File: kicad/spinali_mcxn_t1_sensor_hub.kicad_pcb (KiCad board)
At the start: 2 copper layers, 25 parts, among them U11 BMP390, U13 SK9822-EC20, U14 MPM3822CGRH-Z, U15 TJA1462ATK, U16 PCMF3USB3S, U17 LM74700, U2 MIC5504-1.8YMT, U3 MIC28514T-E/PHA, U4 ICM-45686, U5 MCXN947VDFT, U7 IST8310, U8 TJA1462ATK, U9 TJA1103AHN

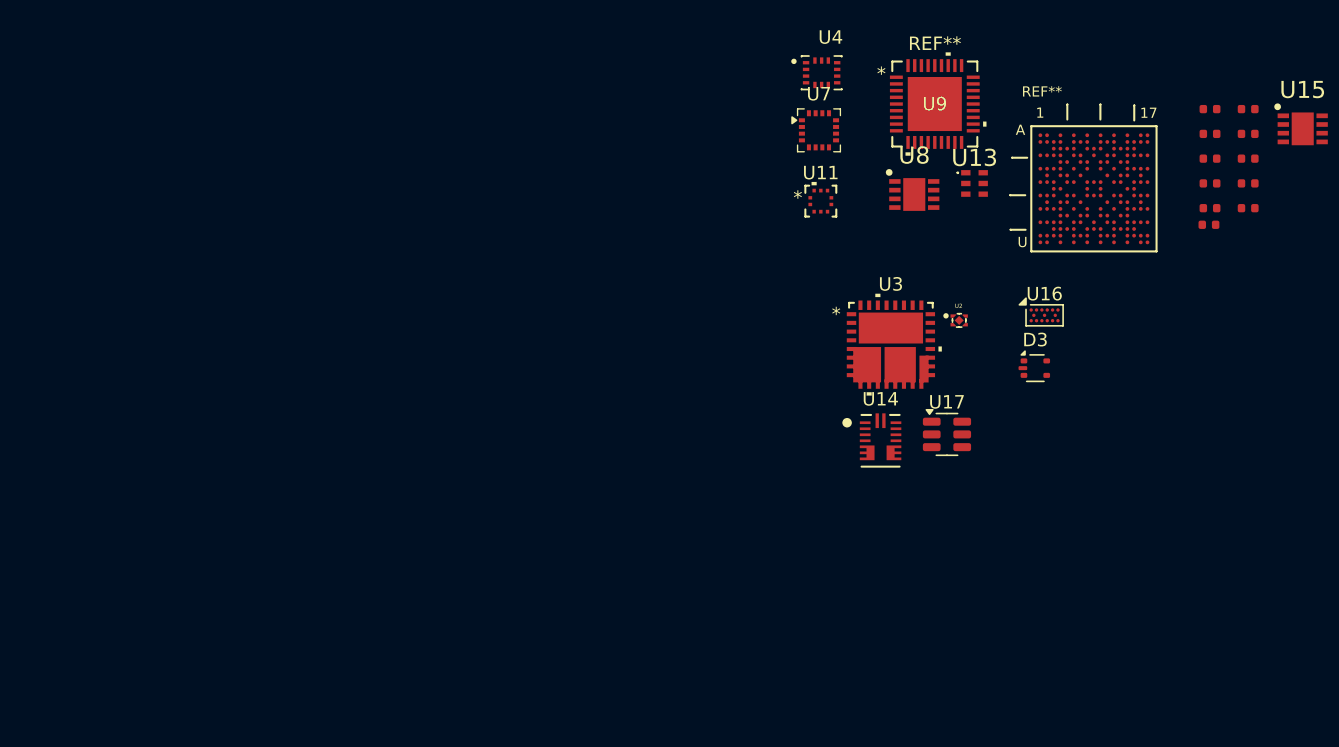
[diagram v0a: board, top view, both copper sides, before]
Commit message: Updated schematics and BOM.
- Finished power supply schematics
- Added power schematic around MCXN
- Assigned MCXN pins
- Created board-to-board schematic and assigned pins to DF40T board-to-board connector
- Added correct sensors, finished sensor schematic
- Updated parts in communication schematic
- Added all part numbers etc in parts parameters
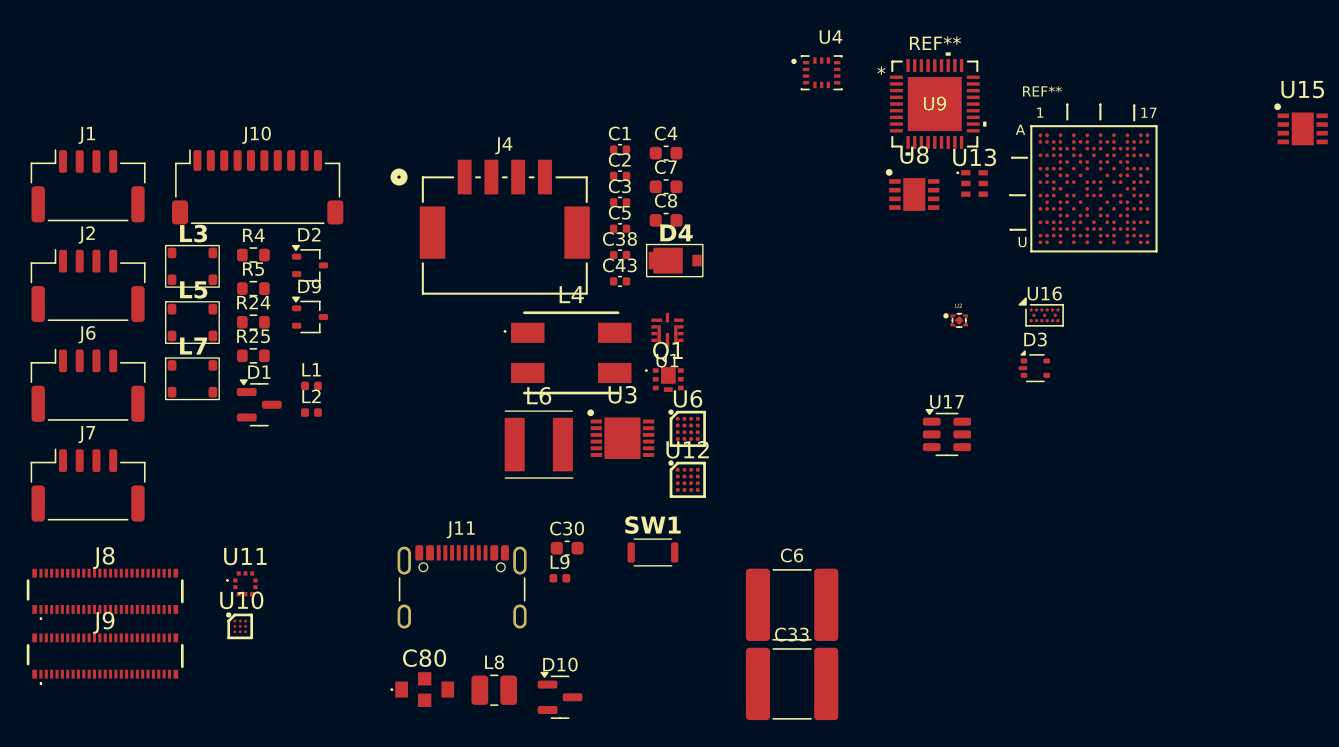
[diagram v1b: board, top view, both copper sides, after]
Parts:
- removed C10, C11, C13, C19: 1uF, PCM_JLCPCB:C_0402
- removed C12, C14, C15, C17, C18, C9: 100nF, PCM_JLCPCB:C_0402
- removed C16: 10uF, PCM_JLCPCB:C_0402
- removed U14: MPM3822CGRH-Z, Power:QFN_2p5x3p5x1p6_MNP
- removed U7: IST8310, Package_LGA:LGA-16_3x3mm_P0.5mm
- added C1: 1nF 100V, Capacitor_SMD:C_0402_1005Metric, F.Cu at (119.8, 88.0)
- added C2: 1nF 16V, Capacitor_SMD:C_0402_1005Metric, F.Cu at (119.8, 90.0)
- added C3: 10nF 16V, Capacitor_SMD:C_0402_1005Metric, F.Cu at (119.8, 91.9)
- added C30: 1uF 10V, Capacitor_SMD:C_0603_1608Metric, F.Cu at (115.8, 117.8)
- added C33: 22uF 100V, Capacitor_SMD:C_2220_5750Metric, F.Cu at (132.7, 127.9)
- added C38: 1nF 100V, Capacitor_SMD:C_0402_1005Metric, F.Cu at (119.8, 95.9)
- added C4: 1uF 25V, Capacitor_SMD:C_0603_1608Metric, F.Cu at (123.2, 88.3)
- added C43: 1nF 16V, Capacitor_SMD:C_0402_1005Metric, F.Cu at (119.8, 97.8)
- added C5: 22nF 10V, Capacitor_SMD:C_0402_1005Metric, F.Cu at (119.8, 93.9)
- added C6: 22uF 100V, Capacitor_SMD:C_2220_5750Metric, F.Cu at (132.7, 122.0)
- added C7: 1uF 10V, Capacitor_SMD:C_0603_1608Metric, F.Cu at (123.2, 90.8)
- added C8: 1uF 10V, Capacitor_SMD:C_0603_1608Metric, F.Cu at (123.2, 93.3)
- added C80: 15nF 50V, Capacitors:NFM31HK103R1H3L, F.Cu at (105.2, 128.3)
- added D1: VETH100A203S-G3-18, Package_TO_SOT_SMD:SOT-23, F.Cu at (92.8, 107.1)
- added D10: BAT54C, Package_TO_SOT_SMD:SOT-23, F.Cu at (115.3, 128.9)
- added D2: PESD2IVN24-UX, Package_TO_SOT_SMD:SOT-323_SC-70, F.Cu at (96.6, 96.6)
- added D4: 6DFN62CA-M3/I, Diodes:DFN3820A, F.Cu at (124.5, 96.3)
- added D9: PESD2IVN24-UX, Package_TO_SOT_SMD:SOT-323_SC-70, F.Cu at (96.6, 100.5)
- added J1: CAN1A, Connector_JST:JST_GH_SM04B-GHS-TB_1x04-1MP_P1.25mm_Horizontal, F.Cu at (80.1, 90.7)
- added J10: Debug, Connector_JST:JST_SH_SM10B-SRSS-TB_1x10-1MP_P1.00mm_Horizontal, F.Cu at (92.7, 90.8)
- added J11: USB4105-GF-A, Connector_USB:USB_C_Receptacle_GCT_USB4105-xx-A_16P_TopMnt_Horizontal, F.Cu at (108.0, 121.8)
- added J2: CAN1B, Connector_JST:JST_GH_SM04B-GHS-TB_1x04-1MP_P1.25mm_Horizontal, F.Cu at (80.1, 98.2)
- added J4: 5055780421, Connectors:CONN_5055780421_MOL, F.Cu at (111.2, 94.4)
- added J6: CAN0A, Connector_JST:JST_GH_SM04B-GHS-TB_1x04-1MP_P1.25mm_Horizontal, F.Cu at (80.1, 105.6)
- added J7: CAN0B, Connector_JST:JST_GH_SM04B-GHS-TB_1x04-1MP_P1.25mm_Horizontal, F.Cu at (80.1, 113.1)
- added J8: DF40TC-50DP-0.4V(51), Connectors:DF40TC-50DP-0.4V(51), F.Cu at (81.3, 121.0)
- added J9: DF40TC-50DP-0.4V(51), Connectors:DF40TC-50DP-0.4V(51), F.Cu at (81.3, 125.8)
- added L1: 600 Ohm, Inductor_SMD:L_0402_1005Metric, F.Cu at (96.8, 105.7)
- added L2: 600 Ohm, Inductor_SMD:L_0402_1005Metric, F.Cu at (96.8, 107.6)
- added L3: IFLN1210BEER512N, Inductors:IFLN1210BEER512N, F.Cu at (86.3, 95.7)
- added L4: ACM7060-301-2PL-TL01, Inductors:ACM70603012PLTL01, F.Cu at (116.2, 103.2)
- added L5: IFLN1210BEER512N, Inductors:IFLN1210BEER512N, F.Cu at (86.3, 99.9)
- added L6: VLS5045EX-330M-H, Inductors:VLS5045EX330M, F.Cu at (113.7, 110.0)
- added L7: IFLN1210BEER512N, Inductors:IFLN1210BEER512N, F.Cu at (86.3, 104.1)
- added L8: 1.5uH, Inductor_SMD:L_1008_2520Metric, F.Cu at (110.4, 128.4)
- added L9: 120 Ohm, Inductor_SMD:L_0402_1005Metric, F.Cu at (115.3, 120.0)
- added Q1: BUK6D56-60EX, MOSFETs:BUK6D5660EX, F.Cu at (123.4, 105.2)
- added R24: 60.4R 1% 1/3W, Resistor_SMD:R_0603_1608Metric, F.Cu at (92.4, 100.9)
- added R25: 60.4R 1% 1/3W, Resistor_SMD:R_0603_1608Metric, F.Cu at (92.4, 103.4)
- added R4: 60.4R 1% 1/3W, Resistor_SMD:R_0603_1608Metric, F.Cu at (92.4, 95.9)
- added R5: 60.4R 1% 1/3W, Resistor_SMD:R_0603_1608Metric, F.Cu at (92.4, 98.4)
- added SW1: SW_SPST, Switches:TS2306A, F.Cu at (122.3, 118.1)
- added U1: MPM3811GG-Z, Power:QFN2x2x1p6_MPM3811_MNP, F.Cu at (123.3, 101.5)
- added U10: BMM350, Sensors:BGA9C40P3X3_128X128X54, F.Cu at (91.4, 123.6)
- added U12: NX5P3363UKZ, NXP_BGA:BGA16C50P4X4_220X220X60, F.Cu at (124.9, 112.7)
- added U6: NX5P3363UKZ, NXP_BGA:BGA16C50P4X4_220X220X60, F.Cu at (124.9, 108.9)
- U11: value BMP390 -> BMP581; footprint Sensors:10LGA_2X2X0p75_BOSCH -> Sensors:BMP581
- U3: value MIC28514T-E/PHA -> LM5160DNTJ; footprint Power:VQFN32_PHA_MCH -> Power:SON50P400X400X100-13N
- moved U11 51.6 mm to (91.8, 120.4)
- moved U3 21.2 mm to (120.0, 109.6)
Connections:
- net /Communication/FC6_P0_I2C_SDA renamed /Communication/P0_8/FLEXIO0_D0
- net /Communication/FC6_P1_I2C_SCK renamed /Communication/P0_9/FLEXIO0_D1
- net /MCU IO Part 1/CAN0_RXD renamed /MCU IO Part 1/P1_19
- net /MCU IO Part 1/CAN0_TXD renamed /MCU IO Part 1/P1_18/FC3_P6
- net /MCU IO Part 1/DEBUG_TCLK_SWCLK renamed /MCU IO Part 1/P0_1/DEBUG_TCLK_SWCLK
- net /MCU IO Part 1/DEBUG_TDI renamed /MCU IO Part 1/P0_3/DEBUG_TDI
- net /MCU IO Part 1/DEBUG_TDO_SWO renamed /MCU IO Part 1/P0_2/DEBUG_TDO_SWO
- net /MCU IO Part 1/DEBUG_TMS_SWDIO renamed /MCU IO Part 1/P0_0/DEBUG_TMS_SWDIO
- net /MCU IO Part 1/ENET0_MDC renamed /MCU IO Part 1/P1_2/FC3_P2
- net /MCU IO Part 1/ENET0_MDIO renamed /MCU IO Part 1/P1_3/FC3_P3
- net /MCU IO Part 1/ENET0_RXCLK renamed /MCU IO Part 1/P1_11
- net /MCU IO Part 1/ENET0_RXD0 renamed /MCU IO Part 1/P1_14/ENET0_RXD0
- net /MCU IO Part 1/ENET0_RXD1 renamed /MCU IO Part 1/P1_15/ENET0_RXD1
- net /MCU IO Part 1/ENET0_RXDV renamed /MCU IO Part 1/P1_13/ENET0_RXDV
- net /MCU IO Part 1/ENET0_RXER renamed /MCU IO Part 1/P1_12/ENET0_RXER
- net /MCU IO Part 1/ENET0_TXCLK renamed /MCU IO Part 1/P1_4/ENET0_TXCLK
- net /MCU IO Part 1/ENET0_TXD0 renamed /MCU IO Part 1/P1_6/ENET0_TXD0
- net /MCU IO Part 1/ENET0_TXD1 renamed /MCU IO Part 1/P1_7/ENET0_TXD1
- net /MCU IO Part 1/ENET0_TXEN renamed /MCU IO Part 1/P1_5/ENET0_TXEN
- net /MCU IO Part 1/ENET0_TXER renamed /MCU IO Part 1/P1_10/ENET0_TXER
- net /MCU IO Part 1/FC0_P0_SPI_SDO renamed /MCU IO Part 1/P0_12/FC1_P4
- net /MCU IO Part 1/FC0_P1_SPI_SCK renamed /MCU IO Part 1/P0_13/FC1_P5
- net /MCU IO Part 1/FC0_P2_SPI_SDI renamed /MCU IO Part 1/P0_14/FC1_P6
- net /MCU IO Part 1/FC0_P3_SPI_CS0 renamed /MCU IO Part 1/P0_15
- net /MCU IO Part 1/FC0_P5_SPI_CS2 renamed /MCU IO Part 1/P0_29
- net /MCU IO Part 1/FC0_P6_SPI_CS1 renamed /MCU IO Part 1/P0_30
- net /MCU IO Part 1/FC1_P0_SPI_SDO renamed /MCU IO Part 1/P0_24/FC1_P0
- net /MCU IO Part 1/FC1_P1_SPI_SCK renamed /MCU IO Part 1/P0_25/FC1_P1
- net /MCU IO Part 1/FC1_P2_SPI_SDI renamed /MCU IO Part 1/P0_26/FC1_P2
- net /MCU IO Part 1/FC1_P3_SPI_CS0 renamed /MCU IO Part 1/P0_27/FC1_P3
- net /MCU IO Part 1/FC1_P4_SPI_CS3 renamed /MCU IO Part 1/P0_28
- net /MCU IO Part 1/FC3_P0_I2C_SDA renamed /MCU IO Part 1/P1_0/FC3_P0
- net /MCU IO Part 1/FC3_P1_I2C_SCL renamed /MCU IO Part 1/P1_1/FC3_P1
- net /MCU IO Part 1/FC4_P0_SPI_SDO renamed /MCU IO Part 1/P1_20/ENET0_MDC
- net /MCU IO Part 1/FC4_P1_SPI_SCK renamed /MCU IO Part 1/P1_21/ENET0_MDIO
- net /MCU IO Part 1/FC4_P2_SPI_SDI renamed /MCU IO Part 1/P1_22/FC4_P2
- net /MCU IO Part 1/FC4_P3_SPI_CS0 renamed /MCU IO Part 1/P1_23/FC4_P3
- net /MCU IO Part 1/MCU_P2_0 renamed /MCU IO Part 1/P2_0/SDHC0_D5
- net /MCU IO Part 1/MCU_P2_1 renamed /MCU IO Part 1/P2_1/SDHC0_D4
- net /MCU IO Part 1/MCU_P2_10 renamed /MCU IO Part 1/P2_10/TRACE_DATA2
- net /MCU IO Part 1/MCU_P2_11 renamed /MCU IO Part 1/P2_11/TRACE_DATA3
- net /MCU IO Part 1/MCU_P2_2 renamed /MCU IO Part 1/P2_2/SDHC0_D1
- net /MCU IO Part 1/MCU_P2_3 renamed /MCU IO Part 1/P2_3/SDHC0_D0
- net /MCU IO Part 1/MCU_P2_4 renamed /MCU IO Part 1/P2_4/SDHC0_CLK
- net /MCU IO Part 1/MCU_P2_5 renamed /MCU IO Part 1/P2_5/SDHC0_CMD
- net /MCU IO Part 1/MCU_P2_6 renamed /MCU IO Part 1/P2_6/SDHC0_D3
- net /MCU IO Part 1/MCU_P2_7 renamed /MCU IO Part 1/P2_7/SDHC0_D2
- net /MCU IO Part 1/MCU_P2_8 renamed /MCU IO Part 1/P2_8/SDHC0_D7
- net /MCU IO Part 1/MCU_P2_9 renamed /MCU IO Part 1/P2_9/SDHC0_D6
- net /MCU IO Part 2/CAN1_RXD renamed /MCU IO Part 2/P4_15/CAN1_RXD
- net /MCU IO Part 2/CAN1_TXD renamed /MCU IO Part 2/P4_16/CAN1_TXD
- net /MCU IO Part 2/FC2_P0_I2C_SDA renamed /MCU IO Part 2/P4_0/FC2_P0
- net /MCU IO Part 2/FC2_P1_I2C_SCL renamed /MCU IO Part 2/P4_1/FC2_P1
- net /MCU IO Part 2/FC6_P0_I2C_SDA renamed /MCU IO Part 2/P3_20
- net /MCU IO Part 2/FC6_P1_I2C_SCK renamed /MCU IO Part 2/P3_21/FLEXIO0_D29
- net /MCU IO Part 2/FC7_P0_I2C_SDA renamed /MCU IO Part 2/P3_2/FC7_P0
- net /MCU IO Part 2/FC7_P1_I2C_SCL renamed /MCU IO Part 2/P3_3/FC7_P1
- net /MCU IO Part 2/FC7_P2_UART_TX renamed /MCU IO Part 2/P3_4/FC7_P2
- net /MCU IO Part 2/FC7_P3_UART_RX renamed /MCU IO Part 2/P3_5/FC7_P3
- net /MCU IO Part 2/FC8_P0_SPI_SDO renamed /MCU IO Part 2/P3_14/FC8_P0
- net /MCU IO Part 2/FC8_P1_SPI_SCK renamed /MCU IO Part 2/P3_15/FC8_P1
- net /MCU IO Part 2/FC8_P2_SPI_SDI renamed /MCU IO Part 2/P3_16/FC8_P2
- net /MCU IO Part 2/FC8_P3_SPI_CS0 renamed /MCU IO Part 2/P3_17/FC8_P3
- U11 pad 1: unconnected-(U11-VDDIO-Pad1) -> +3V3
- U11 pad 10: unconnected-(U11-VDD-Pad10) -> +3V3
- U11 pad 2: unconnected-(U11-SCK-Pad2) -> /Sensors/P0_21/I3C0_SCL
- U11 pad 3: Net-(U11-VSS-Pad3) -> GND
- U11 pad 5: unconnected-(U11-SDO-Pad5) -> /Sensors/P0_20/I3C0_SDA
- U11 pad 6: unconnected-(U11-CSB-Pad6) -> GND
- U11 pad 8: Net-(U11-VSS-Pad3) -> GND
- U11 pad 9: Net-(U11-VSS-Pad3) -> GND
- U3 pad 1: Net-(U3-I_LIM) -> GND
- U3 pad 10: +BATT -> Net-(U3-BST)
- U3 pad 11: +BATT -> Net-(C3-Pad2)
- U3 pad 12: Net-(C37-Pad1) -> Net-(C3-Pad2)
- U3 pad 13: Net-(C37-Pad1) -> GND
- U3 pad 3: Net-(C37-Pad1) -> +BATT
- U3 pad 5: +BATT -> Net-(U3-RON)
- U3 pad 6: +BATT -> Net-(U3-SS)
- U3 pad 7: +BATT -> GND
- U3 pad 8: +BATT -> Net-(U3-FB)
- U3 pad 9: +BATT -> Net-(U3-VCC)
- U4 pad 1: unconnected-(U4-AP_SDO/AP_AD0-Pad1) -> /Sensors/P3_16/FC8_P2
- U4 pad 12: unconnected-(U4-AP_CS-Pad12) -> /Sensors/P3_17/FC8_P3
- U4 pad 13: unconnected-(U4-AP_SCL/AP_SCLK-Pad13) -> /Sensors/P3_15/FC8_P1
- U4 pad 14: unconnected-(U4-AP_SDA/AP_SDIO/AP_SDI-Pad14) -> /Sensors/P3_14/FC8_P0
- U4 pad 4: unconnected-(U4-INT1/INT-Pad4) -> /Sensors/P3_22/FC8_P6
- U4 pad 5: unconnected-(U4-VDDIO-Pad5) -> +3V3
- U4 pad 6: unconnected-(U4-GND-Pad6) -> GND
- U4 pad 8: unconnected-(U4-VDD-Pad8) -> +3V3
- U5 pad A1: unconnected-(U5B-P1_8/TSI0_CH17/ADC1_A8/TRACE_DATA0/FC4_P0/FC5_P4/CT_INP8/SCT0_OUT2/FLEXIO0_D16/EZH_PIO4/PLU_OUT0/ENET0_TXD2/I3C1_SDA/TP_DATA0/WUU0_IN10/LPTMR1_ALT3-PadA1) -> /MCU IO Part 1/P1_8/I3C1_SDA/FC4_P0
- U5 pad A10: unconnected-(U5A-P0_17/TSI0_CH12/ADC0_A9/FC0_P1/CT0_MAT1/UTICK_CAP3/FLEXIO0_D1/PDM0_DATA0/I3C0_SCL/TP_HREADY-PadA10) -> /MCU IO Part 1/P0_17/FC0_P1
- U5 pad A12: unconnected-(U5A-P0_9/ADC0_B9/FC0_P5/CT_INP1/FLEXIO0_D1-PadA12) -> /MCU IO Part 1/P0_9/FLEXIO0_D1
- U5 pad A14: unconnected-(U5A-P0_5/TSI0_CH9/EWM0_OUT_b/FC0_P1/FC1_P5/CT0_MAT3/UTICK_CAP3/PDM0_DATA0-PadA14) -> /MCU IO Part 1/P0_5
- U5 pad A8: unconnected-(U5A-P0_21/TSI0_CH16/ADC0_A13/FC0_P5/FC1_P1/CT_INP1/FLEXIO0_D5/I3C0_SCL-PadA8) -> /MCU IO Part 1/P0_21/I3C0_SCL
- U5 pad B1: unconnected-(U5B-P1_9/TSI0_CH18/ADC1_A9/TRACE_DATA1/FC4_P1/FC5_P5/CT_INP9/SCT0_OUT3/FLEXIO0_D17/EZH_PIO5/PLU_OUT1/ENET0_TXD3/I3C1_SCL/TP_DATA1-PadB1) -> /MCU IO Part 1/P1_9/I3C1_SCL/FC4_P1
- U5 pad B10: unconnected-(U5A-P0_16/TSI0_CH11/ADC0_A8/FC0_P0/CT0_MAT0/UTICK_CAP2/FLEXIO0_D0/PDM0_CLK/I3C0_SDA/TP_HRESP/WUU0_IN2-PadB10) -> /MCU IO Part 1/P0_16/FC0_P0
- U5 pad B11: unconnected-(U5A-P0_11/ADC0_B11/CT0_MAT1/FLEXIO0_D3/HSCMP2_OUT-PadB11) -> /MCU IO Part 1/P0_11
- U5 pad B12: unconnected-(U5A-P0_10/ADC0_B10/FC0_P6/CT0_MAT0/FLEXIO0_D2-PadB12) -> /MCU IO Part 1/P0_10
- U5 pad B14: unconnected-(U5A-P0_4/TSI0_CH8/EWM0_IN/FC0_P0/FC1_P4/CT0_MAT2/UTICK_CAP2/HSCMP1_OUT/PDM0_CLK/WUU0_IN0-PadB14) -> /MCU IO Part 1/P0_4
- U5 pad B17: unconnected-(U5D-P3_0/TRIG_IN0/FC7_P3/CT_INP16/PWM0_A0/FLEXIO0_D8/EZH_PIO0/FLEXSPI0_A_SS0_b/PF_QSPI_CS0_DIS/TP_HWRITE/WUU0_IN22-PadB17) -> /MCU IO Part 2/P3_0/SmartDMA_PIO0
- U5 pad B7: unconnected-(U5A-P0_23/ADC0_A15/CMP2_IN2/EWM0_OUT_b/FC1_P3/CT_INP3/FLEXIO0_D7/WUU0_IN5-PadB7) -> /MCU IO Part 1/P0_23/CMP2_IN2
- U5 pad B8: unconnected-(U5A-P0_22/ADC0_A14/CMP1_IN2/EWM0_IN/FC0_P6/FC1_P2/CT_INP2/FLEXIO0_D6/I3C0_PUR-PadB8) -> /MCU IO Part 1/P0_22/FC0_P6
- U5 pad C10: unconnected-(U5A-P0_18/TSI0_CH13/ADC0_A10/EWM0_IN/FC0_P2/CT0_MAT2/FLEXIO0_D2/HSCMP0_OUT/PDM0_DATA1-PadC10) -> /MCU IO Part 1/P0_18/FC0_P2
- U5 pad C12: unconnected-(U5A-P0_8/ADC0_B8/FC0_P4/CT_INP0/FLEXIO0_D0-PadC12) -> /MCU IO Part 1/P0_8/FLEXIO0_D0
- U5 pad C13: unconnected-(U5A-P0_7/CMP2_IN1/FC0_P3/CT_INP3/WUU0_IN1-PadC13) -> /MCU IO Part 1/P0_7/FC0_P3
- U5 pad C14: /MCU IO Part 1/ISPMODE_N -> /MCU IO Part 1/P0_6/ISPMODE_N
- U5 pad C15: unconnected-(U5D-P3_1/TRIG_IN1/FC6_P0/FC7_P6/CT_INP17/PWM0_B0/FLEXIO0_D9/EZH_PIO1/FLEXSPI0_A_SS1_b/PF_QSPI_CS1_DIS/FREQME_CLK_OUT0-PadC15) -> /MCU IO Part 2/P3_1/FC6_P0
- U5 pad C8: unconnected-(U5A-P0_20/TSI0_CH15/ADC0_A12/FC0_P4/FC1_P0/CT_INP0/FLEXIO0_D4/I3C0_SDA/WUU0_IN4-PadC8) -> /MCU IO Part 1/P0_20/I3C0_SDA
- U5 pad C9: unconnected-(U5A-P0_19/TSI0_CH14/ADC0_A11/EWM0_OUT_b/FC0_P3/CT0_MAT3/FLEXIO0_D3/HSCMP1_OUT/WUU0_IN3-PadC9) -> /MCU IO Part 1/P0_19
- U5 pad D14: unconnected-(U5D-P3_7/FC6_P6/FC7_P1/CT4_MAT3/PWM0_B1/FLEXIO0_D15/EZH_PIO7/FLEXSPI0_A_SCLK/SIM0_VCCEN/SAI0_MCLK/PF_QSPI_SCKIN/TP_LOAD_EN-PadD14) -> /MCU IO Part 2/P3_7/SmartDMA_PIO7
- U5 pad D17: unconnected-(U5D-P3_6/CLKOUT/FC6_P1/CT4_MAT2/PWM0_A1/FLEXIO0_D14/EZH_PIO6/FLEXSPI0_A_DQS/SIM1_VCCEN/SAI1_MCLK/PF_QSPI_CS_n/FREQME_CLK_OUT1/ADC0_CONV_CLK-PadD17) -> /MCU IO Part 2/P3_6/FC6_P1
- U5 pad D7: unconnected-(U5A-P0_31/ADC0_B23/CT_INP3-PadD7) -> /MCU IO Part 1/P0_31
- U5 pad E14: unconnected-(U5D-P3_8/FC6_P4/FC7_P0/CT_INP4/PWM0_A2/FLEXIO0_D16/EZH_PIO8/FLEXSPI0_A_DATA0/SIM0_PD/SAI0_TX_BCLK/PF_QSPI_DATA0/TP_ADDR0/WUU0_IN23-PadE14) -> /MCU IO Part 2/P3_8/SmartDMA_PIO8
- U5 pad F15: unconnected-(U5D-P3_9/FC6_P5/FC7_P2/CT_INP5/PWM0_B2/FLEXIO0_D17/EZH_PIO9/FLEXSPI0_A_DATA1/SIM0_RST/SAI0_TX_FS/PF_QSPI_DATA1/TP_ADDR1-PadF15) -> /MCU IO Part 2/P3_9/SmartDMA_PIO9
- U5 pad F16: unconnected-(U5D-P3_11/FC6_P3/FC7_P5/CT1_MAT1/PWM0_B3/FLEXIO0_D19/EZH_PIO11/FLEXSPI0_A_DATA3/SIM0_IO/SAI0_RXD0/PF_QSPI_DATA3/USB1_TSTI_TX_LS_EN/TP_ADDR3/WUU0_IN24-PadF16) -> /MCU IO Part 2/P3_11/FC6_P3
- U5 pad F17: unconnected-(U5D-P3_10/FC6_P2/FC7_P4/CT1_MAT0/PWM0_A3/FLEXIO0_D18/EZH_PIO10/FLEXSPI0_A_DATA2/SIM0_CLK/SAI0_TXD0/PF_QSPI_DATA2/USB1_TSTI_TX_HS_MODE/TP_ADDR2-PadF17) -> /MCU IO Part 2/P3_10/FC6_P2
- U5 pad F3: unconnected-(U5G-RESET_b-PadF3) -> Net-(U5G-RESET_b)
- U5 pad F4: unconnected-(U5B-P1_17/ADC1_A17/FC5_P1/FC3_P5/CT_INP13/SCT0_OUT7/FLEXIO0_D25/EZH_PIO13/PLU_OUT5/ENET0_RXD3/I3C1_SCL-PadF4) -> /MCU IO Part 1/P1_17/FC3_P5
- U5 pad F6: unconnected-(U5B-P1_16/ADC1_A16/FC5_P0/FC3_P4/CT_INP12/SCT0_OUT6/FLEXIO0_D24/EZH_PIO12/PLU_OUT4/ENET0_RXD2/I3C1_SDA/WUU0_IN14-PadF6) -> /MCU IO Part 1/P1_16/FC3_P4
- U5 pad G11: unconnected-(U5H-VDD_P3_1-PadG11) -> +3V3
- U5 pad G16: unconnected-(U5D-P3_12/FC7_P4/FC6_P4/CT1_MAT2/PWM1_A0/FLEXIO0_D20/EZH_PIO12/FLEXSPI0_A_DATA4/SAI0_RXD1/USB1_TSTI_TX_ENAB/ADC0_CONV_DATA0-PadG16) -> /MCU IO Part 2/P3_12/FC7_P4
- U5 pad G7: unconnected-(U5H-VDD_1-PadG7) -> +3V3
- U5 pad H10: unconnected-(U5H-VDD_P3_2-PadH10) -> +3V3
- U5 pad H12: unconnected-(U5H-VDD_P3_3-PadH12) -> +3V3
- U5 pad H16: unconnected-(U5D-P3_13/FC7_P5/FC6_P5/CT1_MAT3/PWM1_B0/FLEXIO0_D21/EZH_PIO13/FLEXSPI0_A_DATA5/SAI0_TXD1/PF_SPI_CS0_n/USB1_TSTI_TX_HIZ/ADC0_CONV_DATA1-PadH16) -> /MCU IO Part 2/P3_13/FC6_P5
- U5 pad H6: unconnected-(U5H-VDD_2-PadH6) -> +3V3
- U5 pad H8: unconnected-(U5H-VDD_3-PadH8) -> +3V3
- U5 pad K10: unconnected-(U5H-VDD_CORE_1-PadK10) -> Net-(U5H-VDD_CORE_1)
- U5 pad K12: unconnected-(U5F-P5_5/ADC1_B13/TRIG_IN10/LPTMR0_ALT2/TAMPER3-PadK12) -> /MCU IO Part 2/P5_5
- U5 pad K13: unconnected-(U5F-P5_6/ADC1_B14/TRIG_OUT6/LPTMR1_ALT2/TAMPER4-PadK13) -> /MCU IO Part 2/P5_6
- U5 pad K16: unconnected-(U5D-P3_18/FC6_P6/CT2_MAT0/PWM1_X0/FLEXIO0_D26/EZH_PIO18/SAI1_RX_BCLK-PadK16) -> /MCU IO Part 2/P3_18/FC6_P6
- U5 pad K17: unconnected-(U5D-P3_19/FC7_P6/CT2_MAT1/PWM1_X1/FLEXIO0_D27/EZH_PIO19/SAI1_RX_FS-PadK17) -> /MCU IO Part 2/P3_19/FC7_P6
- U5 pad K6: unconnected-(U5H-VDD_LDO_CORE-PadK6) -> Net-(U5H-VDD_CORE_1)
- U5 pad K8: unconnected-(U5H-VDD_P2_1-PadK8) -> +3V3
- U5 pad L11: unconnected-(U5H-VDD_CORE_2-PadL11) -> Net-(U5H-VDD_CORE_1)
- U5 pad L13: unconnected-(U5F-P5_7/ADC1_B15/TRIG_IN11/TAMPER5-PadL13) -> /MCU IO Part 2/P5_7
- U5 pad L14: unconnected-(U5F-P5_8/ADC1_B16/TRIG_OUT7/TAMPER6-PadL14) -> /MCU IO Part 2/P5_8
- U5 pad L7: unconnected-(U5H-VDD_P2_2-PadL7) -> +3V3
- U5 pad M10: unconnected-(U5F-P5_2/ADC1_B10/VBAT_WAKEUP_b/SPC_LPREQ/TAMPER0-PadM10) -> /MCU IO Part 2/P5_2
- U5 pad M12: unconnected-(U5F-P5_4/ADC1_B12/TRIG_OUT7/SPC_LPREQ/TAMPER2-PadM12) -> /MCU IO Part 2/P5_4
- U5 pad M14: unconnected-(U5F-P5_9/ADC1_B17/TAMPER7-PadM14) -> /MCU IO Part 2/P5_9
- U5 pad M15: unconnected-(U5D-P3_23/FC6_P3/CT_INP11/PWM1_X3/FLEXIO0_D31/EZH_PIO23/SAI1_TXD1-PadM15) -> /MCU IO Part 2/P3_23
- U5 pad M16: unconnected-(U5D-P3_22/FC8_P6/FC6_P2/CT_INP10/PWM1_X2/FLEXIO0_D30/EZH_PIO22/SIM0_VCCEN/SAI1_RXD1-PadM16) -> /MCU IO Part 2/P3_22/FC8_P6
- U5 pad M6: unconnected-(U5E-P4_4/FC2_P4/CT_INP14/EZH_PIO28/PLU_IN4/SINC0_MCLK4-PadM6) -> /MCU IO Part 2/P4_4
- U5 pad M8: unconnected-(U5E-P4_5/FC2_P5/CT_INP15/EZH_PIO29/PLU_IN5/SINC0_MBIT4-PadM8) -> /MCU IO Part 2/P4_5
- U5 pad N10: unconnected-(U5E-P4_18/CT3_MAT2/FLEXIO0_D26/PLU_OUT6-PadN10) -> /MCU IO Part 2/P4_18
- U5 pad N11: unconnected-(U5F-P5_3/ADC1_B11/TRIG_IN11/RTC_CLKOUT/TAMPER1-PadN11) -> /MCU IO Part 2/P5_3
- U5 pad N14: unconnected-(U5H-VDD_SYS/VOUT_SYS-PadN14) -> Net-(U5H-VDD_SYS/VOUT_SYS)
- U5 pad N5: unconnected-(U5H-VDD_P4_1-PadN5) -> +3V3
- U5 pad N7: unconnected-(U5E-P4_6/TRIG_OUT4/FC2_P6/CT_INP18/EZH_PIO30/PLU_CLK-PadN7) -> /MCU IO Part 2/P4_6
- U5 pad N8: unconnected-(U5E-P4_14/CT4_MAT2/FLEXIO0_D22/PLU_OUT2-PadN8) -> /MCU IO Part 2/P4_14
- U5 pad P15: unconnected-(U5H-VDD_LDO_SYS-PadP15) -> +3V3
- U5 pad P17: unconnected-(U5H-DCDC_LX/DCDC_LX-PadP17) -> Net-(U5H-DCDC_LX/DCDC_LX)
- U5 pad P3: unconnected-(U5G-ANA_0/ADC0_A0-PadP3) -> /MCU IO USB & Power/ANA_0
- U5 pad P4: unconnected-(U5H-VDD_P4_2-PadP4) -> +3V3
- U5 pad R10: unconnected-(U5E-P4_19/OPAMP1_OUT/ADC0_B1/CMP1_IN4P/TRIG_OUT5/CT3_MAT3/FLEXIO0_D27/PLU_OUT7/SINC0_MCLK_OUT1-PadR10) -> /MCU IO Part 2/P4_19
- U5 pad R12: unconnected-(U5H-VDD_USB-PadR12) -> +3V3
- U5 pad R15: unconnected-(U5H-VDD_DCDC-PadR15) -> +3V3
- U5 pad R3: unconnected-(U5G-ANA_1/ADC0_B0-PadR3) -> /MCU IO USB & Power/ANA_1
- U5 pad R4: unconnected-(U5H-VDD_ANA-PadR4) -> Net-(U5H-VDD_ANA)
- U5 pad R5: unconnected-(U5H-VREFH-PadR5) -> Net-(U5H-VDD_ANA)
- U5 pad R6: unconnected-(U5H-VREFL-PadR6) -> GND
- U5 pad R9: unconnected-(U5E-P4_17/OPAMP1_INP1/ADC0_B6/TRIG_IN9/FC2_P3/USB1_OTG_OC/CT3_MAT1/FLEXIO0_D25/PLU_OUT5/SINC0_MBIT1-PadR9) -> /MCU IO Part 2/P4_17
- U5 pad T1: unconnected-(U5E-P4_2/DAC0_OUT/ADC0_A4/ADC1_A4/CMP0_IN4N/CMP1_IN4N/CMP2_IN4N/TRIG_IN6/FC2_P2/CT_INP12/EZH_PIO26/PLU_IN2/SINC0_MBIT3-PadT1) -> /MCU IO Part 2/P4_2/FC2_P2
- U5 pad T10: unconnected-(U5E-P4_20/OPAMP2_INP0/ADC1_A6/TRIG_IN8/FC2_P4/CT2_MAT0/FLEXIO0_D28/SINC0_MCLK2-PadT10) -> /MCU IO Part 2/P4_20/FC2_P4
- U5 pad T11: unconnected-(U5E-P4_21/OPAMP2_INP1/ADC1_B6/TRIG_IN9/FC2_P5/CT2_MAT1/FLEXIO0_D29/SINC0_MBIT2-PadT11) -> /MCU IO Part 2/P4_21
- U5 pad T12: unconnected-(U5E-P4_22/CT2_MAT2/FLEXIO0_D30-PadT12) -> /MCU IO Part 2/P4_22
- U5 pad T17: unconnected-(U5H-VDD_BAT-PadT17) -> Net-(U5H-VDD_BAT)
- U5 pad T2: unconnected-(U5G-ANA_4/ADC1_A0-PadT2) -> /MCU IO USB & Power/ANA_4
- U5 pad T3: unconnected-(U5G-ANA_5/ADC1_B0-PadT3) -> /MCU IO USB & Power/ANA_5
- U5 pad T4: unconnected-(U5E-P4_7/CT_INP19/EZH_PIO31-PadT4) -> /MCU IO Part 2/P4_7
- U5 pad T6: unconnected-(U5E-P4_12/OPAMP0_INP0/ADC0_A5/ADC1_A5/USB0_VBUS_DET/FC2_P0/CT4_MAT0/FLEXIO0_D20/PLU_OUT0/SINC0_MCLK0/CAN0_RXD/MTR_START_BURNIN/WUU0_IN20-PadT6) -> /MCU IO Part 2/P4_12/CAN0_RXD
- U5 pad T7: unconnected-(U5E-P4_13/OPAMP0_INP1/ADC0_B5/ADC1_B5/TRIG_IN8/FC2_P1/USB1_ID/CT4_MAT1/FLEXIO0_D21/PLU_OUT1/SINC0_MBIT0/CAN0_TXD-PadT7) -> /MCU IO Part 2/P4_13/CAN0_TXD
- U5 pad U1: unconnected-(U5E-P4_3/DAC1_OUT/ADC0_B4/ADC1_B4/CMP0_IN5N/CMP1_IN5N/CMP2_IN5N/TRIG_IN7/FC2_P3/CT_INP13/EZH_PIO27/PLU_IN3/WUU0_IN19-PadU1) -> /MCU IO Part 2/P4_3/FC2_P3
- U5 pad U10: unconnected-(U5G-ANA_22/OPAMP2_INN-PadU10) -> /MCU IO USB & Power/ANA_22/OPAMP2_INN
- U5 pad U12: unconnected-(U5E-P4_23/OPAMP2_OUT/ADC0_A2/ADC0_B2/ADC1_B3/CMP2_IN4P/TRIG_OUT5/FC2_P6/CT2_MAT3/FLEXIO0_D31/SINC0_MCLK_OUT2-PadU12) -> /MCU IO Part 2/P4_23/FC2_P6
- U5 pad U14: Net-(U5G-USB1_VBUS) -> VBUS
- U5 pad U16: unconnected-(U5F-P5_0/EXTAL32K/ADC1_B8/TRIG_IN10/LPTMR0_ALT2-PadU16) -> /MCU IO Part 2/P5_0/EXTAL32K
- U5 pad U17: unconnected-(U5F-P5_1/XTAL32K/ADC1_B9/TRIG_OUT6/LPTMR1_ALT2-PadU17) -> /MCU IO Part 2/P5_1/XTAL32K
- U5 pad U2: unconnected-(U5G-ANA_6/DAC2_OUT/ADC0_A3/ADC1_A3-PadU2) -> /MCU IO USB & Power/ANA_6/DAC2_OUT
- U5 pad U6: unconnected-(U5G-ANA_14/OPAMP0_INN-PadU6) -> /MCU IO USB & Power/ANA_14
- U5 pad U8: unconnected-(U5G-ANA_18/OPAMP1_INN-PadU8) -> /MCU IO USB & Power/ANA_18
- U8 pad 6: unconnected-(U8-CANL-Pad6) -> Net-(U8-CANL)
- U8 pad 7: unconnected-(U8-CANH-Pad7) -> Net-(U8-CANH)

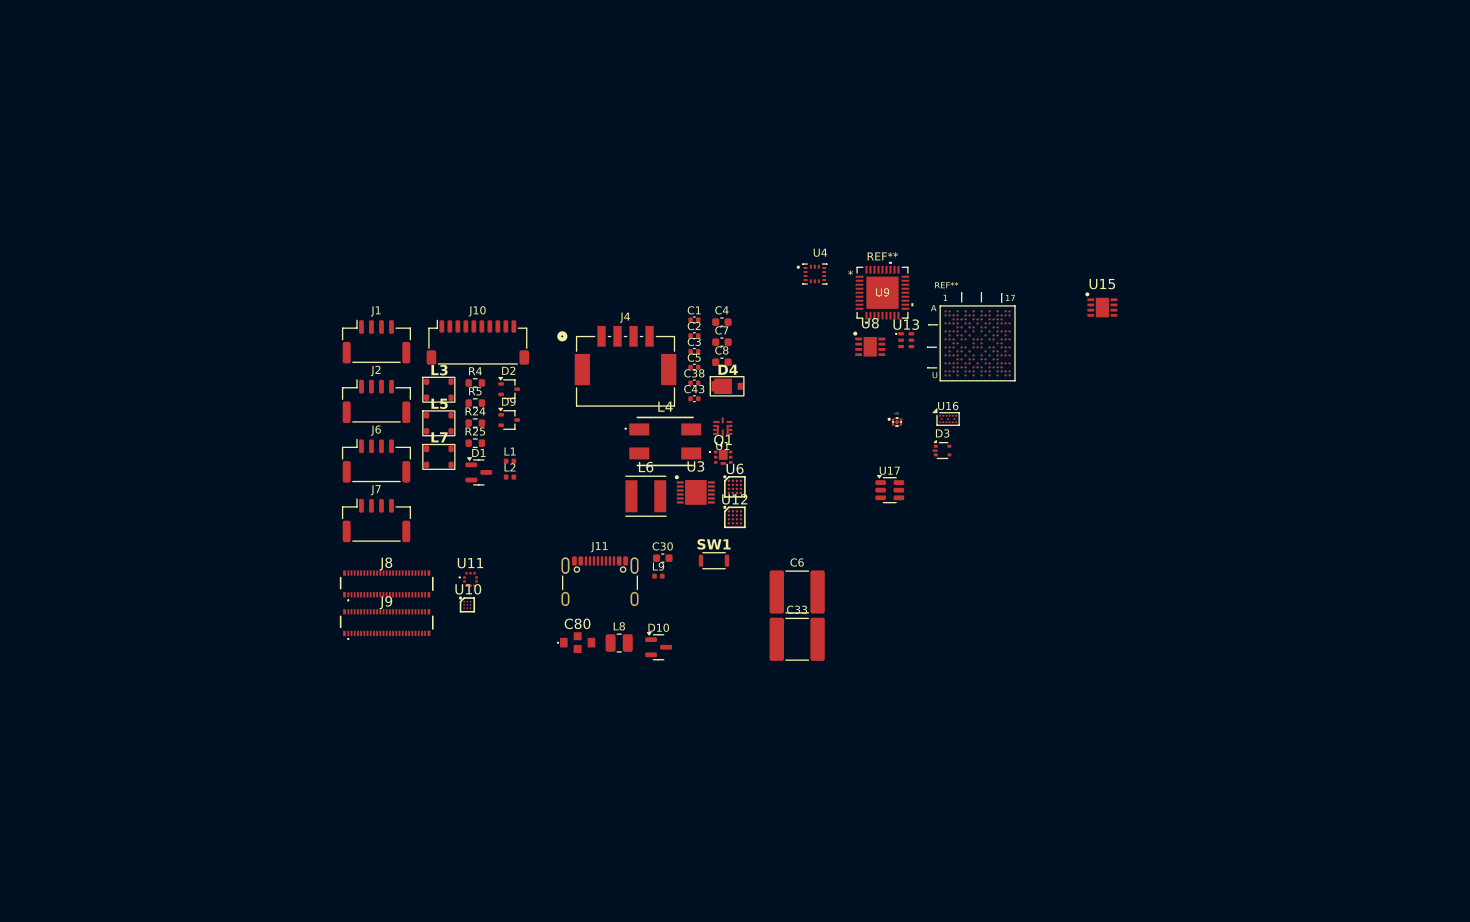
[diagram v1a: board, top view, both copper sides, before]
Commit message: Finished schematic design for first review
Finished schematic design for first review.
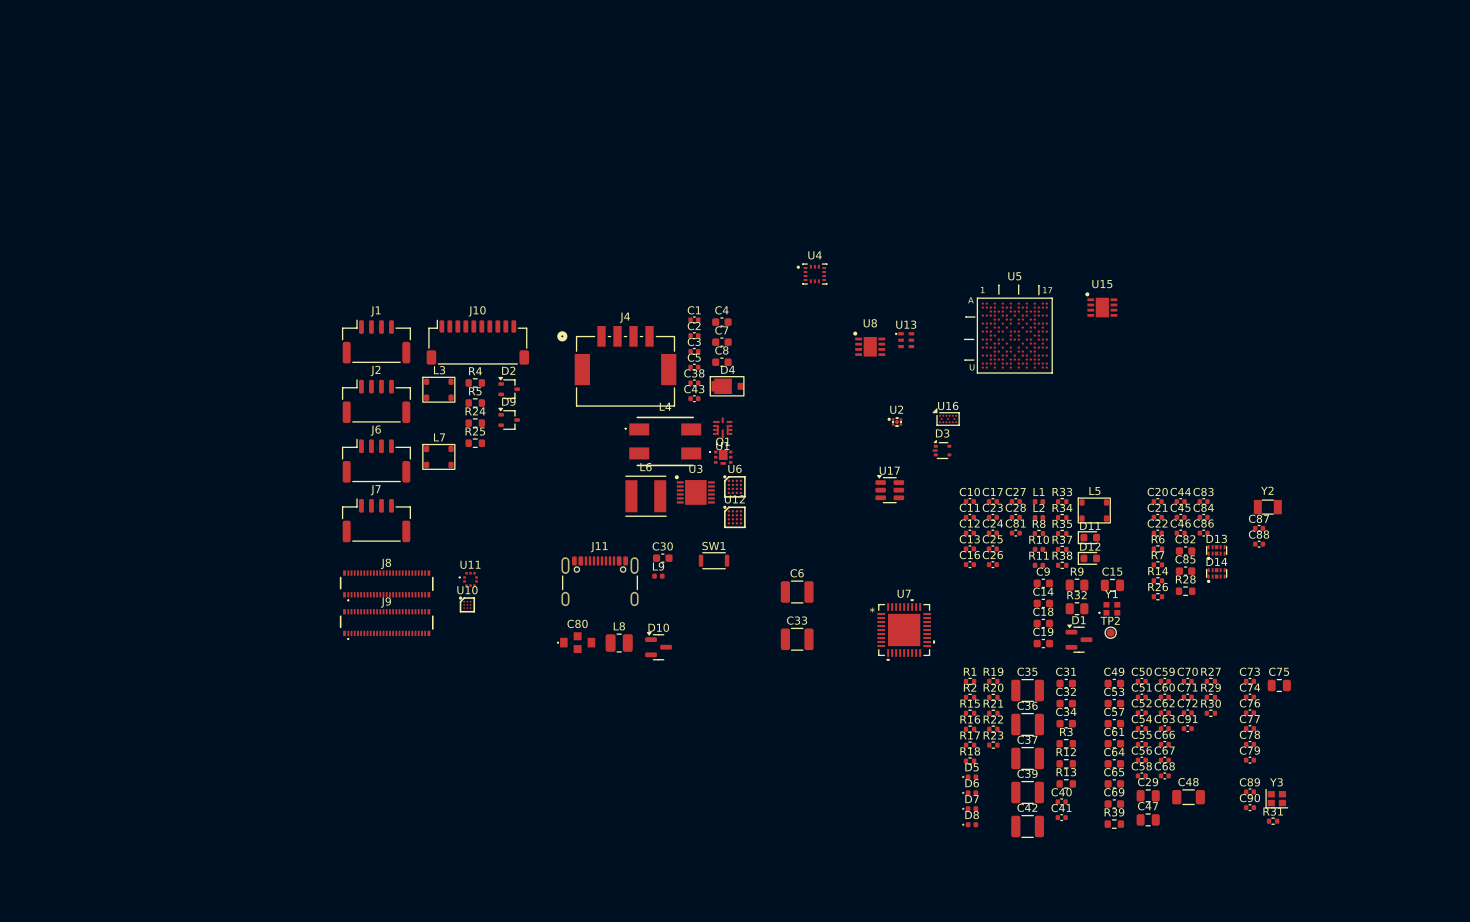
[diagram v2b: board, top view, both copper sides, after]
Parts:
- removed U9: TJA1103AHN, NXP_HV:HVQFN36_SOT1092-2_NXP
- added C10: 100nF 16V, Capacitor_SMD:C_0402_1005Metric, F.Cu at (154.2, 110.7)
- added C11: 100nF 16V, Capacitor_SMD:C_0402_1005Metric, F.Cu at (154.2, 112.7)
- added C12: 100nF 16V, Capacitor_SMD:C_0402_1005Metric, F.Cu at (154.2, 114.6)
- added C13: 100nF 16V, Capacitor_SMD:C_0402_1005Metric, F.Cu at (154.2, 116.6)
- added C14: 1uF 16V, Capacitor_SMD:C_0603_1608Metric, F.Cu at (163.4, 123.4)
- added C15: 10uF 16V, Capacitor_SMD:C_0805_2012Metric, F.Cu at (172.1, 121.2)
- added C16: 100nF 16V, Capacitor_SMD:C_0402_1005Metric, F.Cu at (154.2, 118.6)
- added C17: 100nF 16V, Capacitor_SMD:C_0402_1005Metric, F.Cu at (157.1, 110.7)
- added C18: 1uF 16V, Capacitor_SMD:C_0603_1608Metric, F.Cu at (163.4, 125.9)
- added C19: 1uF 16V, Capacitor_SMD:C_0603_1608Metric, F.Cu at (163.4, 128.4)
- added C20: 4700pF, Capacitor_SMD:C_0402_1005Metric, F.Cu at (177.7, 110.7)
- added C21: 100pF, Capacitor_SMD:C_0402_1005Metric, F.Cu at (177.7, 112.7)
- added C22: 100pF, Capacitor_SMD:C_0402_1005Metric, F.Cu at (177.7, 114.6)
- added C23: 100nF 50V, Capacitor_SMD:C_0402_1005Metric, F.Cu at (157.1, 112.7)
- added C24: 100pF, Capacitor_SMD:C_0402_1005Metric, F.Cu at (157.1, 114.6)
- added C25: 4700pF 50V, Capacitor_SMD:C_0402_1005Metric, F.Cu at (157.1, 116.6)
- added C26: 100pF, Capacitor_SMD:C_0402_1005Metric, F.Cu at (157.1, 118.6)
- added C27: 100nF 50V, Capacitor_SMD:C_0402_1005Metric, F.Cu at (160.0, 110.7)
- added C28: 8pF 16V, Capacitor_SMD:C_0402_1005Metric, F.Cu at (160.0, 112.7)
- added C29: 10uF 10V, Capacitor_SMD:C_0805_2012Metric, F.Cu at (176.5, 147.5)
- added C31: 100nF 100V, Capacitor_SMD:C_0603_1608Metric, F.Cu at (166.3, 133.4)
- added C32: 22nF 100V, Capacitor_SMD:C_0603_1608Metric, F.Cu at (166.3, 135.9)
- added C34: 100nF 100V, Capacitor_SMD:C_0603_1608Metric, F.Cu at (166.3, 138.5)
- added C35: 47uF 16V, Capacitor_SMD:C_1210_3225Metric, F.Cu at (161.4, 134.3)
- added C36: 47uF 16V, Capacitor_SMD:C_1210_3225Metric, F.Cu at (161.4, 138.6)
- added C37: 47uF 16V, Capacitor_SMD:C_1210_3225Metric, F.Cu at (161.4, 142.8)
- added C39: 47uF 16V, Capacitor_SMD:C_1210_3225Metric, F.Cu at (161.4, 147.1)
- added C40: 100nF 16V, Capacitor_SMD:C_0402_1005Metric, F.Cu at (165.7, 148.2)
- added C41: 100nF 16V, Capacitor_SMD:C_0402_1005Metric, F.Cu at (165.7, 150.2)
- added C42: 47uF 16V, Capacitor_SMD:C_1210_3225Metric, F.Cu at (161.4, 151.3)
- added C44: 100pF, Capacitor_SMD:C_0402_1005Metric, F.Cu at (180.6, 110.7)
- added C45: 4700pF, Capacitor_SMD:C_0402_1005Metric, F.Cu at (180.6, 112.7)
- added C46: 100pF, Capacitor_SMD:C_0402_1005Metric, F.Cu at (180.6, 114.6)
- added C47: 2.2uF 16V, Capacitor_SMD:C_0805_2012Metric, F.Cu at (176.5, 150.5)
- added C48: 6.8uF 16V, Capacitor_SMD:C_1206_3216Metric, F.Cu at (181.6, 147.7)
- added C49: 1uF 16V, Capacitor_SMD:C_0603_1608Metric, F.Cu at (172.3, 133.4)
- added C50: 100nF 16V, Capacitor_SMD:C_0402_1005Metric, F.Cu at (175.7, 133.2)
- added C51: 100nF 16V, Capacitor_SMD:C_0402_1005Metric, F.Cu at (175.7, 135.1)
- added C52: 100nF 16V, Capacitor_SMD:C_0402_1005Metric, F.Cu at (175.7, 137.1)
- added C53: 1uF 16V, Capacitor_SMD:C_0603_1608Metric, F.Cu at (172.3, 135.9)
- added C54: 100nF 16V, Capacitor_SMD:C_0402_1005Metric, F.Cu at (175.7, 139.1)
- added C55: 100nF 16V, Capacitor_SMD:C_0402_1005Metric, F.Cu at (175.7, 141.1)
- added C56: 100nF 16V, Capacitor_SMD:C_0402_1005Metric, F.Cu at (175.7, 143.0)
- added C57: 1uF 16V, Capacitor_SMD:C_0603_1608Metric, F.Cu at (172.3, 138.5)
- added C58: 100nF 16V, Capacitor_SMD:C_0402_1005Metric, F.Cu at (175.7, 145.0)
- added C59: 100nF 16V, Capacitor_SMD:C_0402_1005Metric, F.Cu at (178.6, 133.2)
- added C60: 100nF 16V, Capacitor_SMD:C_0402_1005Metric, F.Cu at (178.6, 135.1)
- added C61: 1uF 16V, Capacitor_SMD:C_0603_1608Metric, F.Cu at (172.3, 141.0)
- added C62: 100nF 16V, Capacitor_SMD:C_0402_1005Metric, F.Cu at (178.6, 137.1)
- added C63: 100nF 16V, Capacitor_SMD:C_0402_1005Metric, F.Cu at (178.6, 139.1)
- added C64: 4.7uF 6.3V, Capacitor_SMD:C_0603_1608Metric, F.Cu at (172.3, 143.5)
- added C65: 4.7uF 6.3V, Capacitor_SMD:C_0603_1608Metric, F.Cu at (172.3, 146.0)
- added C66: 100nF 16V, Capacitor_SMD:C_0402_1005Metric, F.Cu at (178.6, 141.1)
- added C67: 100nF 16V, Capacitor_SMD:C_0402_1005Metric, F.Cu at (178.6, 143.0)
- added C68: 100nF 16V, Capacitor_SMD:C_0402_1005Metric, F.Cu at (178.6, 145.0)
- added C69: 1uF 16V, Capacitor_SMD:C_0603_1608Metric, F.Cu at (172.3, 148.5)
- added C70: 100nF 16V, Capacitor_SMD:C_0402_1005Metric, F.Cu at (181.5, 133.2)
- added C71: 100nF 16V, Capacitor_SMD:C_0402_1005Metric, F.Cu at (181.5, 135.1)
- added C72: 100nF 16V, Capacitor_SMD:C_0402_1005Metric, F.Cu at (181.5, 137.1)
- added C73: 100nF 16V, Capacitor_SMD:C_0402_1005Metric, F.Cu at (189.2, 133.2)
- added C74: 100nF 16V, Capacitor_SMD:C_0402_1005Metric, F.Cu at (189.2, 135.1)
- added C75: 2.2uF 16V, Capacitor_SMD:C_0805_2012Metric, F.Cu at (192.9, 133.7)
- added C76: 100nF 16V, Capacitor_SMD:C_0402_1005Metric, F.Cu at (189.2, 137.1)
- added C77: 100nF 16V, Capacitor_SMD:C_0402_1005Metric, F.Cu at (189.2, 139.1)
- added C78: 100nF 16V, Capacitor_SMD:C_0402_1005Metric, F.Cu at (189.2, 141.1)
- added C79: 100nF 16V, Capacitor_SMD:C_0402_1005Metric, F.Cu at (189.2, 143.0)
- added C81: 8pF 16V, Capacitor_SMD:C_0402_1005Metric, F.Cu at (160.0, 114.6)
- added C82: 1uF 10V, Capacitor_SMD:C_0603_1608Metric, F.Cu at (181.2, 116.9)
- added C83: 47nF 10V, Capacitor_SMD:C_0402_1005Metric, F.Cu at (183.5, 110.7)
- added C84: 47nF 10V, Capacitor_SMD:C_0402_1005Metric, F.Cu at (183.5, 112.7)
- added C85: 1uF 10V, Capacitor_SMD:C_0603_1608Metric, F.Cu at (181.2, 119.4)
- added C86: 100nF 16V, Capacitor_SMD:C_0402_1005Metric, F.Cu at (183.5, 114.6)
- added C87: 4.7pF 50V, Capacitor_SMD:C_0402_1005Metric, F.Cu at (190.4, 114.0)
- added C88: 4.7pF 50V, Capacitor_SMD:C_0402_1005Metric, F.Cu at (190.4, 116.0)
- added C89: 4.7pF 50V, Capacitor_SMD:C_0402_1005Metric, F.Cu at (189.2, 147.0)
- added C9: 1uF 16V, Capacitor_SMD:C_0603_1608Metric, F.Cu at (163.4, 120.9)
- added C90: 4.7pF 50V, Capacitor_SMD:C_0402_1005Metric, F.Cu at (189.2, 149.0)
- added C91: 100nF 16V, Capacitor_SMD:C_0402_1005Metric, F.Cu at (181.5, 139.1)
- added D11: LED_AMB, LED_SMD:LED_0603_1608Metric, F.Cu at (169.3, 115.2)
- added D12: LED_GRN, LED_SMD:LED_0603_1608Metric, F.Cu at (169.3, 117.8)
- added D13: ESD7104MUTAG, TVS:ESD8104MUTAG, F.Cu at (185.1, 116.8)
- added D14: ESD7104MUTAG, TVS:ESD8104MUTAG, F.Cu at (185.1, 119.7)
- added D5: 5V-IND, LED_SMD:LED_0402_1005Metric, F.Cu at (154.5, 145.1)
- added D6: 3V3-IND, LED_SMD:LED_0402_1005Metric, F.Cu at (154.5, 147.1)
- added D7: 1V8-IND, LED_SMD:LED_0402_1005Metric, F.Cu at (154.5, 149.1)
- added D8: VBUS, LED_SMD:LED_0402_1005Metric, F.Cu at (154.5, 151.1)
- added R1: 3k3, Resistor_SMD:R_0402_1005Metric, F.Cu at (154.3, 133.2)
- added R10: 680, Inductor_SMD:L_0402_1005Metric, F.Cu at (162.9, 116.7)
- added R11: 680, Inductor_SMD:L_0402_1005Metric, F.Cu at (162.9, 118.7)
- added R12: 68k 75V, Resistor_SMD:R_0603_1608Metric, F.Cu at (166.3, 143.5)
- added R13: 12k 75V, Resistor_SMD:R_0603_1608Metric, F.Cu at (166.3, 146.0)
- added R14: 0, Resistor_SMD:R_0402_1005Metric, F.Cu at (177.7, 120.6)
- added R15: 1k, Resistor_SMD:R_0402_1005Metric, F.Cu at (154.3, 137.2)
- added R16: 1k, Resistor_SMD:R_0402_1005Metric, F.Cu at (154.3, 139.2)
- added R17: 82k 1%, Resistor_SMD:R_0402_1005Metric, F.Cu at (154.3, 141.1)
- added R18: 18k 1%, Resistor_SMD:R_0402_1005Metric, F.Cu at (154.3, 143.1)
- added R19: 100k, Resistor_SMD:R_0402_1005Metric, F.Cu at (157.2, 133.2)
- added R2: 2k2, Resistor_SMD:R_0402_1005Metric, F.Cu at (154.3, 135.2)
- added R20: 2k2, Resistor_SMD:R_0402_1005Metric, F.Cu at (157.2, 135.2)
- added R21: 47k 1%, Resistor_SMD:R_0402_1005Metric, F.Cu at (157.2, 137.2)
- added R22: 2k2, Resistor_SMD:R_0402_1005Metric, F.Cu at (157.2, 139.2)
- added R23: 24k 1%, Resistor_SMD:R_0402_1005Metric, F.Cu at (157.2, 141.1)
- added R26: 0, Resistor_SMD:R_0402_1005Metric, F.Cu at (177.7, 122.6)
- added R27: 10k, Resistor_SMD:R_0402_1005Metric, F.Cu at (184.4, 133.2)
- added R28: 100, Resistor_SMD:R_0603_1608Metric, F.Cu at (181.2, 121.9)
- added R29: 5.1k, Resistor_SMD:R_0402_1005Metric, F.Cu at (184.4, 135.2)
- added R3: 100k 75V, Resistor_SMD:R_0603_1608Metric, F.Cu at (166.3, 141.0)
- added R30: 5.1k, Resistor_SMD:R_0402_1005Metric, F.Cu at (184.4, 137.2)
- added R31: 10k, Resistor_SMD:R_0402_1005Metric, F.Cu at (192.1, 150.7)
- added R32: 1k 2/5W, Resistor_SMD:R_0805_2012Metric, F.Cu at (167.6, 124.1)
- added R33: 0, Resistor_SMD:R_0402_1005Metric, F.Cu at (165.8, 110.7)
- added R34: 10k, Resistor_SMD:R_0402_1005Metric, F.Cu at (165.8, 112.7)
- added R35: 10k, Resistor_SMD:R_0402_1005Metric, F.Cu at (165.8, 114.7)
- added R37: 10k, Resistor_SMD:R_0402_1005Metric, F.Cu at (165.8, 116.7)
- added R38: 10k, Resistor_SMD:R_0402_1005Metric, F.Cu at (165.8, 118.7)
- added R39: 100, Resistor_SMD:R_0603_1608Metric, F.Cu at (172.3, 151.0)
- added R6: 0, Resistor_SMD:R_0402_1005Metric, F.Cu at (177.7, 116.6)
- added R7: 0, Resistor_SMD:R_0402_1005Metric, F.Cu at (177.7, 118.6)
- added R8: 0, Resistor_SMD:R_0402_1005Metric, F.Cu at (162.9, 114.7)
- added R9: 1k 2/5W, Resistor_SMD:R_0805_2012Metric, F.Cu at (167.6, 121.1)
- added TP2: ENET_REFCLK, TestPoint:TestPoint_Pad_D1.0mm, F.Cu at (171.8, 127.1)
- added U7: TJA1103AHN, NXP_HV:HVQFN36_SOT1092-2_NXP, F.Cu at (146.0, 126.7)
- added Y1: 25MHz, Crystals:XRCGB25M000F3A00R0, F.Cu at (172.0, 124.1)
- added Y2: 32.768kHz, Crystal:Crystal_SMD_3215-2Pin_3.2x1.5mm, F.Cu at (191.5, 111.4)
- added Y3: 24MHz, Crystal:Crystal_SMD_2016-4Pin_2.0x1.6mm, F.Cu at (192.6, 147.8)
- C33, C6: value 22uF 100V -> 10uF 100V; footprint Capacitor_SMD:C_2220_5750Metric -> Capacitor_SMD:C_1210_3225Metric
- moved L5 82.7 mm to (168.3, 110.8)
- moved D1 77.9 mm to (167.9, 128.0)
- moved L1 66.3 mm to (162.9, 110.7)
- moved L2 66.3 mm to (162.9, 112.7)
- moved U5 4.75 mm to (159.9, 90.0)
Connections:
- net /MCU IO Part 1/P0_31 renamed /MCU IO Part 1/P0_31/ENET0_WAKE_IN_OUT
- net /MCU IO Part 1/P1_19 renamed /MCU IO Part 1/P1_19/ENET0_INT_N
- net /MCU IO Part 1/P1_4/ENET0_TXCLK renamed /MCU IO Part 1/P1_4/ENET0_REFCLK
- net /Power supplies/T1_TRX_M renamed /Power supplies/ENET_TRX_M
- net /Power supplies/T1_TRX_P renamed /Power supplies/ENET_TRX_P
- D1 pad 1: /Communication/T1_TRX_P -> /Ethernet PHY/ENET_TRX_P
- D1 pad 2: /Communication/T1_TRX_M -> /Ethernet PHY/ENET_TRX_M
- J10 pad 9: /Communication/P0_5 -> /Communication/RESET_b
- L1 pad 2: Net-(U9-VDDA_AO) -> VDDIO
- L2 pad 2: VDDIO -> Net-(U7-VDDA_AO)
- L5 pad 1: /Communication/TRX_P -> /Ethernet PHY/TRX_P
- L5 pad 4: /Communication/TRX_M -> /Ethernet PHY/TRX_M
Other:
- copper layers 2 -> 4
